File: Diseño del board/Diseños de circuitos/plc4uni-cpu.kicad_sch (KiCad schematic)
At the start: 1 part, among them U2 ESP32-S3-MINI-1U

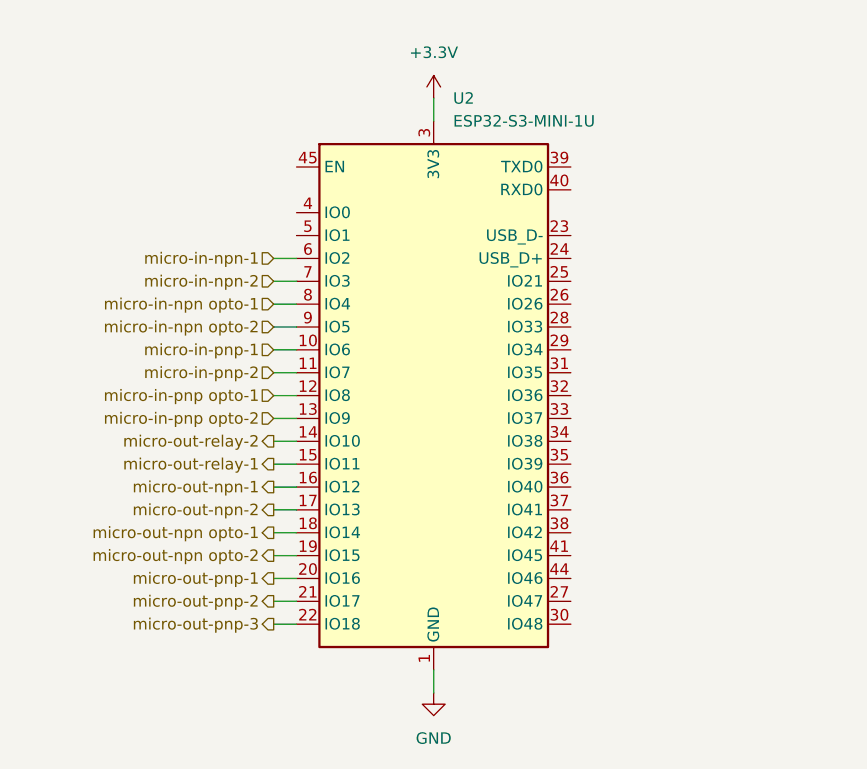
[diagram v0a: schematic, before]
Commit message: se agrego entrada y salida 0-10V
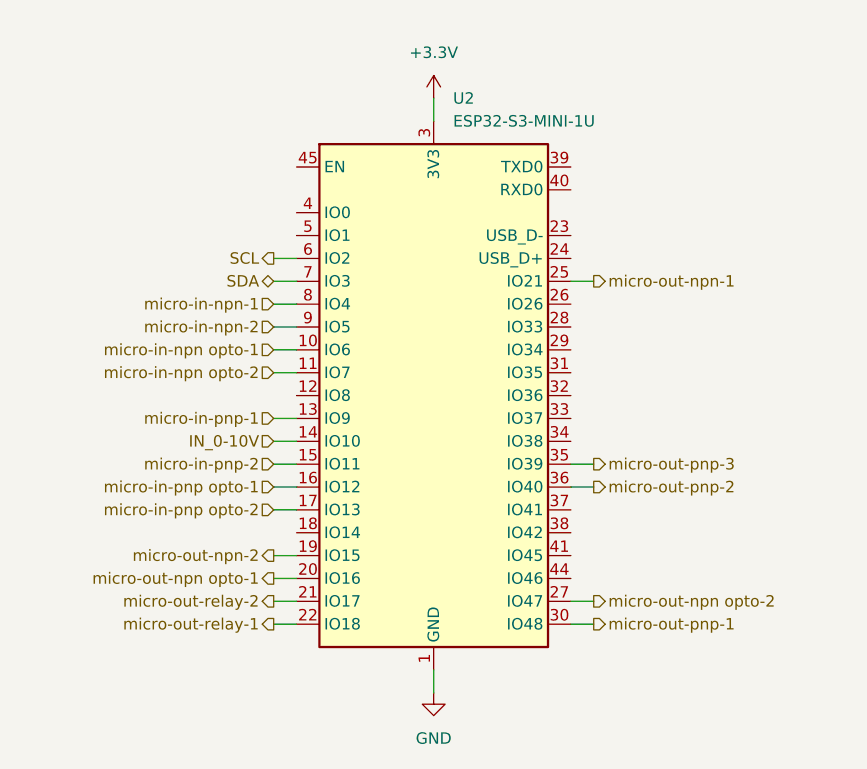
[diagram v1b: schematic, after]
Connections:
- net micro-in-npn opto-1: now also U2.10 (IO6); no longer U2.8 (IO4)
- net micro-in-npn opto-2: now also U2.11 (IO7); no longer U2.9 (IO5)
- net micro-in-npn-1: now also U2.8 (IO4); no longer U2.6 (IO2)
- net micro-in-npn-2: now also U2.9 (IO5); no longer U2.7 (IO3)
- net micro-in-pnp opto-1: now also U2.16 (IO12); no longer U2.12 (IO8)
- net micro-in-pnp opto-2: now also U2.17 (IO13); no longer U2.13 (IO9)
- net micro-in-pnp-1: now also U2.13 (IO9); no longer U2.10 (IO6)
- net micro-in-pnp-2: now also U2.15 (IO11); no longer U2.11 (IO7)
- net micro-out-npn opto-1: now also U2.20 (IO16); no longer U2.18 (IO14)
- net micro-out-npn opto-2: now also U2.27 (IO47); no longer U2.19 (IO15)
- net micro-out-npn-1: now also U2.25 (IO21); no longer U2.16 (IO12)
- net micro-out-npn-2: now also U2.19 (IO15); no longer U2.17 (IO13)
- net micro-out-pnp-1: now also U2.30 (IO48); no longer U2.20 (IO16)
- net micro-out-pnp-2: now also U2.36 (IO40); no longer U2.21 (IO17)
- net micro-out-pnp-3: now also U2.35 (IO39); no longer U2.22 (IO18)
- net micro-out-relay-1: now also U2.22 (IO18); no longer U2.15 (IO11)
- net micro-out-relay-2: now also U2.21 (IO17); no longer U2.14 (IO10)
- new net IN_0-10V: U2.14 (IO10)
- new net SCL: U2.6 (IO2)
- new net SDA: U2.7 (IO3)

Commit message: arreglos
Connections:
- net +3.3V renamed VDD
- no-connect marks 0 -> 20
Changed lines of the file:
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@@
 	(generator_version "9.0")
 	(paper "A4")
+	(no_connect
+		(at 144.78 109.22)
+	)
+	(no_connect
+		(at 144.78 68.58)
+	)
+	(no_connect
+		(at 144.78 71.12)
+	)
+	(no_connect
+		(at 144.78 76.2)
+	)
+	(no_connect
+		(at 144.78 96.52)
+	)
+	(no_connect
+		(at 144.78 114.3)
+	)
+	(no_connect
+		(at 144.78 83.82)
+	)
+	(no_connect
+		(at 144.78 99.06)
+	)
+	(no_connect
+		(at 144.78 91.44)
+	)
+	(no_connect
+		(at 144.78 111.76)
+	)
+	(no_connect
+		(at 144.78 86.36)
+	)
+	(no_connect
+		(at 114.3 68.58)
+	)
+	(no_connect
+		(at 114.3 73.66)
+	)
+	(no_connect
+		(at 144.78 93.98)
+	)
+	(no_connect
+		(at 144.78 78.74)
+	)
+	(no_connect
+		(at 144.78 106.68)
+	)
+	(no_connect
+		(at 144.78 88.9)
+	)
+	(no_connect
+		(at 114.3 109.22)
+	)
+	(no_connect
+		(at 114.3 76.2)
+	)
+	(no_connect
+		(at 114.3 93.98)
+	)
 	(wire
 		(pts
@@
 	(wire
 		(pts
-			(xy 129.54 60.96) (xy 129.54 63.5)
+			(xy 129.54 58.42) (xy 129.54 63.5)
 		)
 		(stroke
@@
 	)
 	(symbol
-		(lib_id "power:+3.3V")
-		(at 129.54 60.96 0)
+		(lib_id "power:VDD")
+		(at 129.54 58.42 0)
 		(unit 1)
 		(exclude_from_sim no)
@@
 		(fields_autoplaced yes)
 		(property "Reference" "#PWR03"
-			(at 129.54 64.77 0)
+			(at 129.54 62.23 0)
 			(effects
 				(font
@@
 			)
 		)
-		(property "Value" "+3.3V"
-			(at 129.54 55.88 0)
+		(property "Value" "VDD"
+			(at 129.54 53.34 0)
 			(effects
 				(font
@@
 		)
 		(property "Footprint" ""
-			(at 129.54 60.96 0)
+			(at 129.54 58.42 0)
 			(effects
 				(font
@@
 		)
 		(property "Datasheet" ""
-			(at 129.54 60.96 0)
+			(at 129.54 58.42 0)
 			(effects
 				(font
@@
 			)
 		)
-		(property "Description" "Power symbol creates a global label with name \"+3.3V\""
-			(at 129.54 60.96 0)
+		(property "Description" "Power symbol creates a global label with name \"VDD\""
+			(at 129.54 58.42 0)
 			(effects
 				(font
